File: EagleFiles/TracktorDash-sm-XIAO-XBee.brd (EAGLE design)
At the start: 48.4 x 45.6 mm, 11 parts

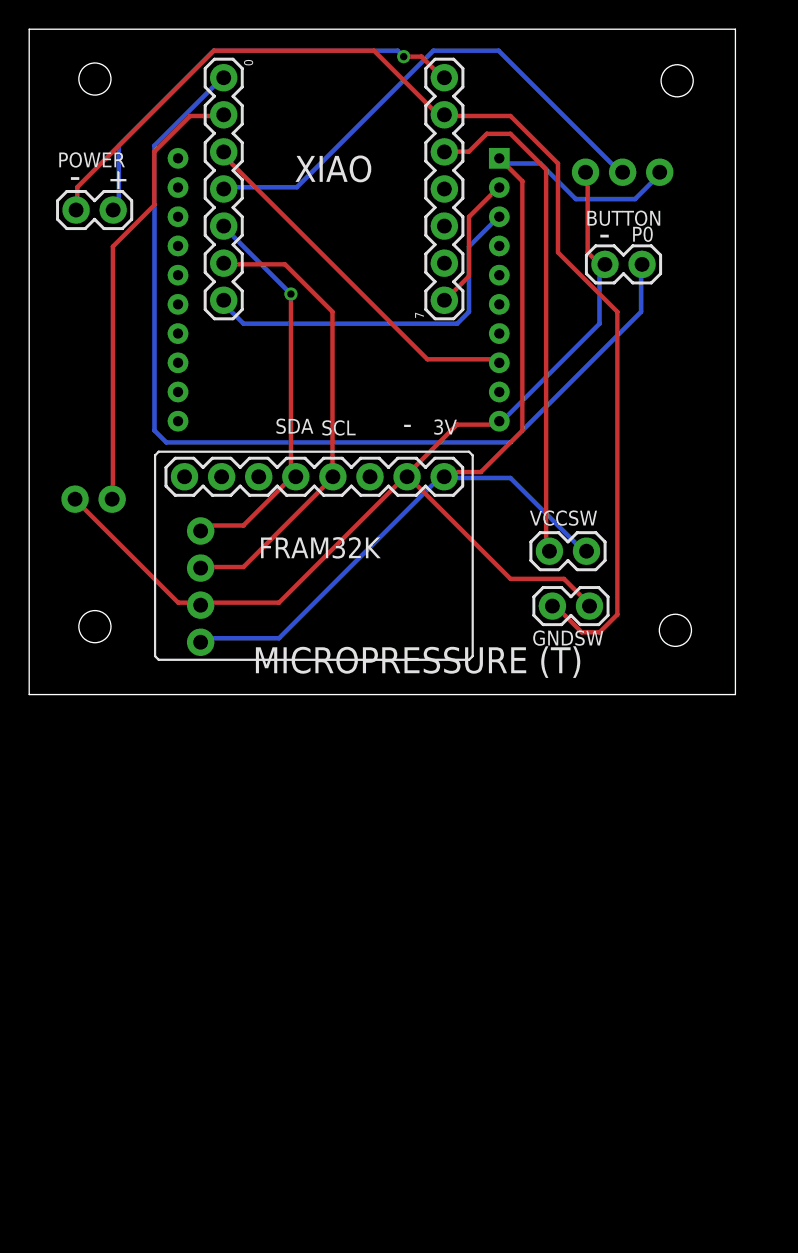
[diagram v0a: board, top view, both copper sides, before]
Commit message: 2ND ORDER PCBWAY
FRAM ORIANTATION AND CONNECTIONS FIXED
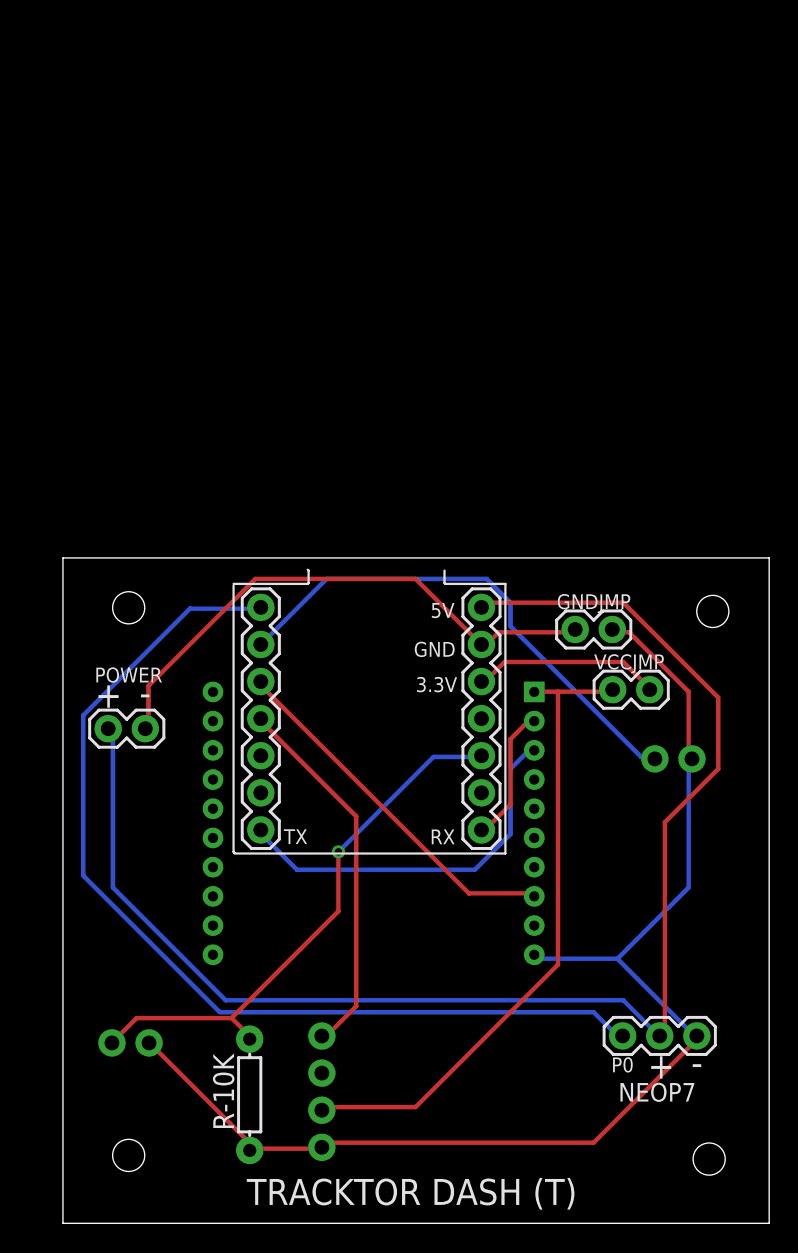
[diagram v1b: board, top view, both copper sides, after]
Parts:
- removed 0, 7: (no value), SparkFun-Connectors:1X07
- removed FRAM32K: FRAM32K, SparkFun-Connectors:1X08
- removed GNDSW, VCCSW: button, SparkFun-Connectors:1X02
- removed LED: LED, SparkFun-Connectors:1X02
- removed MPRESSURE: (no value), SparkFun-Connectors:1X04
- removed UVSENSOR: UV, SparkFun-Connectors:1X03
- added BUZZER: (no value), SparkFun-Connectors:1X04_NO_SILK
- added GNDJMP, VCCJMP, VIBRATION: (no value), SparkFun-Connectors:1X02
- added NEOP7: 455-1750-1-ND, SparkFun-Connectors:1X03
- added R-10K: 10, SparkFun-Resistors:AXIAL-0.3
- added XIAO-1-7, XIAO-8-14: (no value), SparkFun-Connectors:1X07
- POWER: value button -> (none)
- moved XBEES2C 36.6 mm to (15.4, 27.4)
- moved POWER 35.5 mm to (-2.76, 30.4), turned to 0 degrees
- moved BUTTON 34.4 mm to (37.2, 28.3), flipped to the bottom
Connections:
- removed net N$10: 7.5, VCCSW.2
- removed net N$7: 0.1, BUTTON.2
- new net N$12: GNDJMP.1, POWER.2, XIAO-8-14.6
- net GND: now also BUZZER.1, GNDJMP.2, NEOP7.1, R-10K.P$1, VIBRATION.2; no longer FRAM32K.2, GNDSW.1, LED.1, MPRESSURE.2, UVSENSOR.1
- net N$1: now also NEOP7.3, XIAO-1-7.1; no longer 0.5, FRAM32K.5, MPRESSURE.4
- net N$11: now also R-10K.P$2, VIBRATION.1, XIAO-8-14.3; no longer 7.7, POWER.1
- net N$2: now also VCCJMP.2, XIAO-8-14.5; no longer 0.6, FRAM32K.4, MPRESSURE.3
- net N$3: now also XIAO-1-7.7; no longer 0.7
- net N$4: now also BUTTON.2, XIAO-1-7.2; no longer 7.6, GNDSW.2, POWER.2
- net N$5: now also XIAO-1-7.3; no longer 0.3
- net N$6: now also BUZZER.4, XIAO-1-7.4; no longer 0.4, UVSENSOR.2
- net N$8: now also NEOP7.2, POWER.1, XIAO-8-14.7; no longer 0.2, LED.2
- net N$9: now also XIAO-8-14.1; no longer 7.1
- net VCC: now also BUZZER.2, VCCJMP.1; no longer FRAM32K.1, MPRESSURE.1, UVSENSOR.3, VCCSW.1
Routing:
- net N$7: track 66.8 -> 0.00 mm
- net N$8: track 30.8 -> 96.7 mm
- net N$4: track 79.8 -> 34.9 mm
- net N$1: track 27.4 -> 67.7 mm, vias 1 -> 0
- net N$12: track 0.00 -> 37.6 mm
- net N$10: track 34.8 -> 0.00 mm
- net VCC: track 72.3 -> 44.4 mm
- net N$2: track 31.8 -> 12.9 mm
- net GND: track 74.5 -> 85.3 mm
- net N$6: track 34.7 -> 25.6 mm
- net N$11: track 30.3 -> 37.8 mm
- net N$3: track 25.3 -> 26.0 mm
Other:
- board text added: "3.3V"
- board text added: "5V"
- board text added: "GND"
- board text added: "P4"
- board text added: "P9"
- board text added: "RX"
- board text added: "TRACKTOR DASH (B)"
- board text added: "TRACKTOR DASH (T)"
- board text added: "TX"
- board text removed: "3V"
- board text removed: "MICROPRESSURE (B)"
- board text removed: "MICROPRESSURE (T)"
- board text removed: "P3"
- board text removed: "SCL"
- board text removed: "SDA"
- board text removed: "XIAO"
